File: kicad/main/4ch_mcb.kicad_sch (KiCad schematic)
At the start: 19 parts, among them J15 ICSP, J16 MD1, J17 MD2, J18 MD3, J19 MD4, U5 ATmega328P-AU, Y1 8Mhz

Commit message: fix:
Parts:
- renumbered J15 to J14, J16 to J15, J17 to J16, J18 to J17, J19 to J18
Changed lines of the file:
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@@
   (symbol (lib_id "power:GND") (at 138.43 59.69 0) (unit 1)
     (in_bom yes) (on_board yes)
-    (property "Reference" "#PWR051" (id 0) (at 138.43 66.04 0)
+    (property "Reference" "#PWR049" (id 0) (at 138.43 66.04 0)
       (effects (font (size 1.27 1.27)) hide)
     )
@@
   (symbol (lib_id "Connector_Generic:Conn_01x04") (at 195.58 114.3 0) (unit 1)
     (in_bom yes) (on_board yes)
-    (property "Reference" "J18" (id 0) (at 193.4972 106.2482 0))
+    (property "Reference" "J17" (id 0) (at 193.4972 106.2482 0))
     (property "Value" "MD3" (id 1) (at 193.4972 108.5596 0))
     (property "Footprint" "0.main.robot:JSTB4B-ZR" (id 2) (at 195.58 114.3 0)
@@
   (symbol (lib_id "power:GND") (at 154.94 38.1 0) (unit 1)
     (in_bom yes) (on_board yes)
-    (property "Reference" "#PWR053" (id 0) (at 154.94 44.45 0)
+    (property "Reference" "#PWR051" (id 0) (at 154.94 44.45 0)
       (effects (font (size 1.27 1.27)) hide)
     )
@@
   (symbol (lib_id "power:GND") (at 153.67 106.68 0) (unit 1)
     (in_bom yes) (on_board yes)
-    (property "Reference" "#PWR052" (id 0) (at 153.67 113.03 0)
+    (property "Reference" "#PWR050" (id 0) (at 153.67 113.03 0)
       (effects (font (size 1.27 1.27)) hide)
     )
@@
   (symbol (lib_id "power:+3.3VA") (at 68.58 123.19 0) (unit 1)
     (in_bom yes) (on_board yes)
-    (property "Reference" "#PWR046" (id 0) (at 68.58 127 0)
+    (property "Reference" "#PWR044" (id 0) (at 68.58 127 0)
       (effects (font (size 1.27 1.27)) hide)
     )
@@
   (symbol (lib_id "power:+3.3VA") (at 137.16 39.37 0) (unit 1)
     (in_bom yes) (on_board yes) (fields_autoplaced)
-    (property "Reference" "#PWR050" (id 0) (at 137.16 43.18 0)
+    (property "Reference" "#PWR048" (id 0) (at 137.16 43.18 0)
       (effects (font (size 1.27 1.27)) hide)
     )
@@
   (symbol (lib_id "power:GND") (at 68.58 171.45 0) (unit 1)
     (in_bom yes) (on_board yes)
-    (property "Reference" "#PWR047" (id 0) (at 68.58 177.8 0)
+    (property "Reference" "#PWR045" (id 0) (at 68.58 177.8 0)
       (effects (font (size 1.27 1.27)) hide)
     )
@@
   (symbol (lib_id "Connector_Generic:Conn_01x04") (at 195.58 88.9 0) (unit 1)
     (in_bom yes) (on_board yes)
-    (property "Reference" "J17" (id 0) (at 193.4972 80.8482 0))
+    (property "Reference" "J16" (id 0) (at 193.4972 80.8482 0))
     (property "Value" "MD2" (id 1) (at 193.4972 83.1596 0))
     (property "Footprint" "0.main.robot:JSTB4B-ZR" (id 2) (at 195.58 88.9 0)
@@
   (symbol (lib_id "Connector_Generic:Conn_01x04") (at 195.58 48.26 0) (unit 1)
     (in_bom yes) (on_board yes)
-    (property "Reference" "J16" (id 0) (at 193.4972 40.2082 0))
+    (property "Reference" "J15" (id 0) (at 193.4972 40.2082 0))
     (property "Value" "MD1" (id 1) (at 193.4972 42.5196 0))
     (property "Footprint" "0.main.robot:JSTB4B-ZR" (id 2) (at 195.58 48.26 0)
@@
   (symbol (lib_id "power:+3.3VA") (at 93.98 29.21 0) (unit 1)
     (in_bom yes) (on_board yes) (fields_autoplaced)
-    (property "Reference" "#PWR048" (id 0) (at 93.98 33.02 0)
+    (property "Reference" "#PWR046" (id 0) (at 93.98 33.02 0)
       (effects (font (size 1.27 1.27)) hide)
     )
@@
   (symbol (lib_id "power:+3.3VA") (at 158.75 74.93 0) (unit 1)
     (in_bom yes) (on_board yes) (fields_autoplaced)
-    (property "Reference" "#PWR054" (id 0) (at 158.75 78.74 0)
+    (property "Reference" "#PWR052" (id 0) (at 158.75 78.74 0)
       (effects (font (size 1.27 1.27)) hide)
     )
@@
   (symbol (lib_id "Connector_Generic:Conn_01x04") (at 195.58 130.81 0) (unit 1)
     (in_bom yes) (on_board yes)
-    (property "Reference" "J19" (id 0) (at 193.4972 122.7582 0))
+    (property "Reference" "J18" (id 0) (at 193.4972 122.7582 0))
     (property "Value" "MD4" (id 1) (at 193.4972 125.0696 0))
     (property "Footprint" "0.main.robot:JSTB4B-ZR" (id 2) (at 195.58 130.81 0)
@@
   (symbol (lib_id "Connector_Generic:Conn_01x06") (at 147.32 30.48 90) (unit 1)
     (in_bom yes) (on_board yes)
-    (property "Reference" "J15" (id 0) (at 157.1752 31.3944 90)
+    (property "Reference" "J14" (id 0) (at 157.1752 31.3944 90)
       (effects (font (size 1.27 1.27)) (justify right))
     )
@@
   (symbol (lib_id "power:GND") (at 49.53 120.65 0) (unit 1)
     (in_bom yes) (on_board yes)
-    (property "Reference" "#PWR045" (id 0) (at 49.53 127 0)
+    (property "Reference" "#PWR043" (id 0) (at 49.53 127 0)
       (effects (font (size 1.27 1.27)) hide)
     )
@@
   (symbol (lib_id "power:GND") (at 127 96.52 0) (unit 1)
     (in_bom yes) (on_board yes)
-    (property "Reference" "#PWR049" (id 0) (at 127 102.87 0)
-      (effects (font (size 1.27 1.27)) hide)
-    )
+    (property "Reference" "#PWR047" (id 0) (at 127 102.87 0)
+      (effects (font (size 1.27 1.27)) hide)
+    )

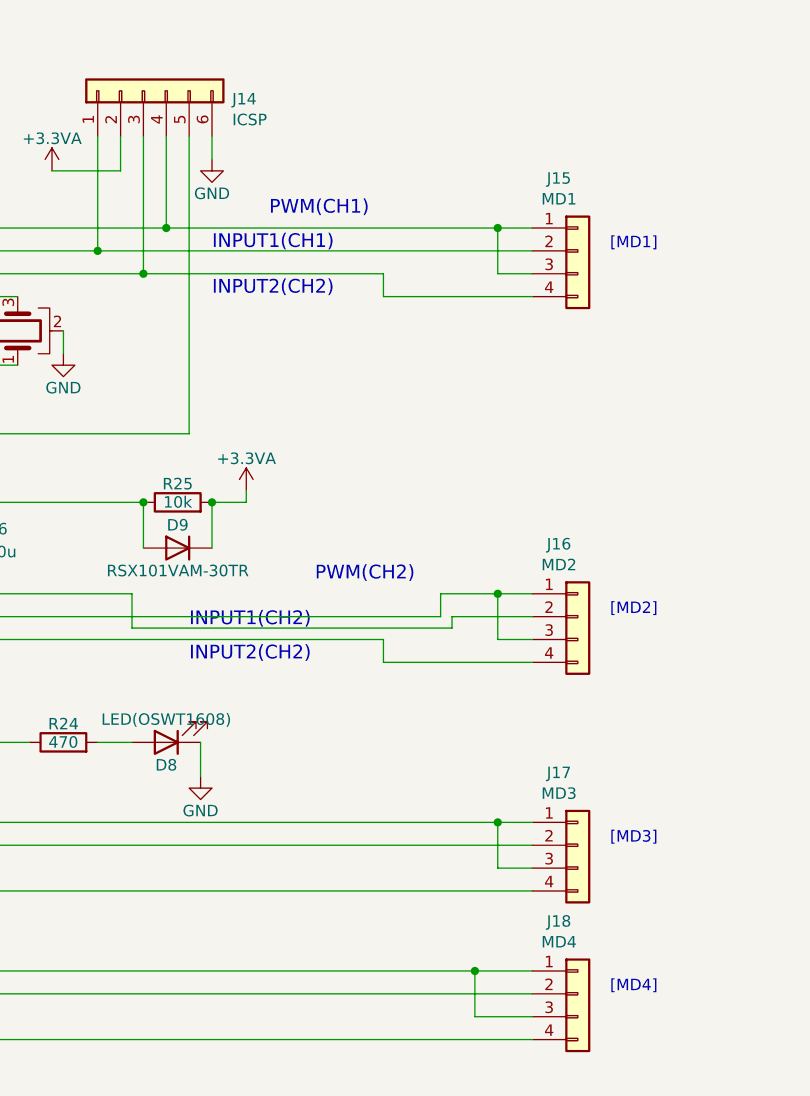
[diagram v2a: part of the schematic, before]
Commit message: fix: vison-board GND
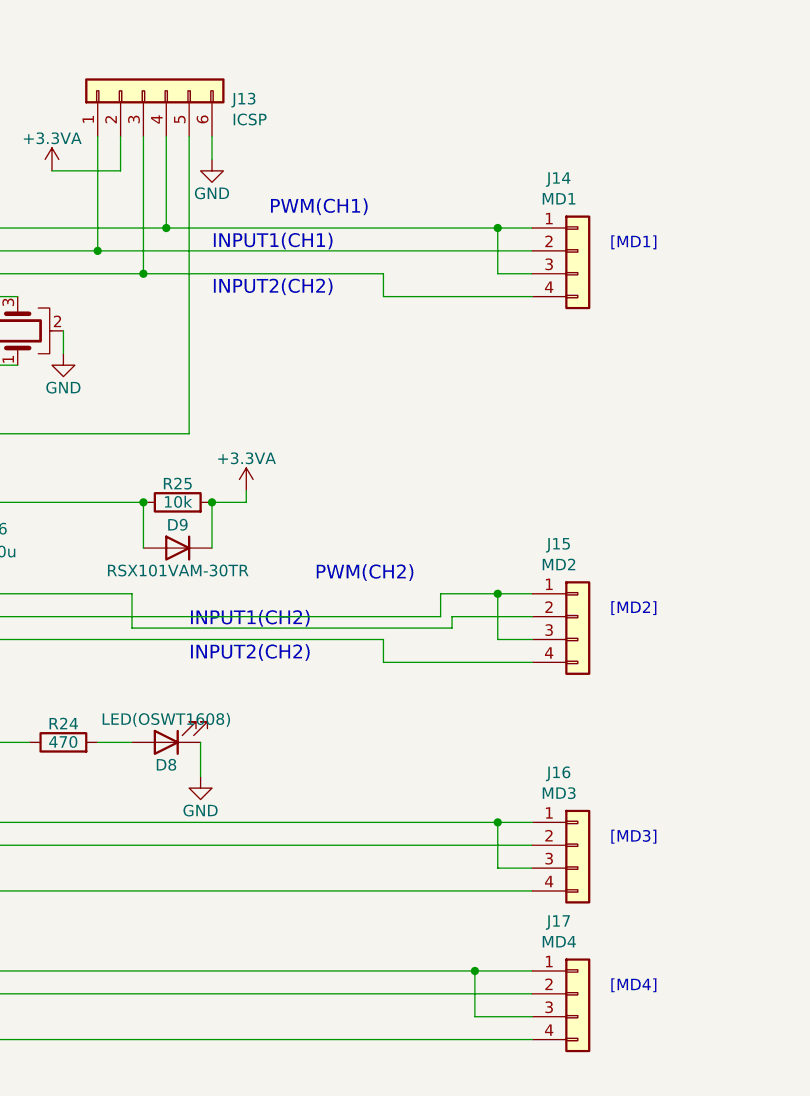
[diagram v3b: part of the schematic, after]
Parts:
- renumbered J14 to J13, J15 to J14, J16 to J15, J17 to J16, J18 to J17
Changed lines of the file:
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@@
   (symbol (lib_id "power:GND") (at 138.43 59.69 0) (unit 1)
     (in_bom yes) (on_board yes)
-    (property "Reference" "#PWR049" (id 0) (at 138.43 66.04 0)
+    (property "Reference" "#PWR048" (id 0) (at 138.43 66.04 0)
       (effects (font (size 1.27 1.27)) hide)
     )
@@
   (symbol (lib_id "Connector_Generic:Conn_01x04") (at 195.58 114.3 0) (unit 1)
     (in_bom yes) (on_board yes)
-    (property "Reference" "J17" (id 0) (at 193.4972 106.2482 0))
+    (property "Reference" "J16" (id 0) (at 193.4972 106.2482 0))
     (property "Value" "MD3" (id 1) (at 193.4972 108.5596 0))
     (property "Footprint" "0.main.robot:JSTB4B-ZR" (id 2) (at 195.58 114.3 0)
@@
   (symbol (lib_id "power:GND") (at 154.94 38.1 0) (unit 1)
     (in_bom yes) (on_board yes)
-    (property "Reference" "#PWR051" (id 0) (at 154.94 44.45 0)
+    (property "Reference" "#PWR050" (id 0) (at 154.94 44.45 0)
       (effects (font (size 1.27 1.27)) hide)
     )
@@
   (symbol (lib_id "power:GND") (at 153.67 106.68 0) (unit 1)
     (in_bom yes) (on_board yes)
-    (property "Reference" "#PWR050" (id 0) (at 153.67 113.03 0)
+    (property "Reference" "#PWR049" (id 0) (at 153.67 113.03 0)
       (effects (font (size 1.27 1.27)) hide)
     )
@@
   (symbol (lib_id "power:+3.3VA") (at 68.58 123.19 0) (unit 1)
     (in_bom yes) (on_board yes)
-    (property "Reference" "#PWR044" (id 0) (at 68.58 127 0)
+    (property "Reference" "#PWR043" (id 0) (at 68.58 127 0)
       (effects (font (size 1.27 1.27)) hide)
     )
@@
   (symbol (lib_id "power:+3.3VA") (at 137.16 39.37 0) (unit 1)
     (in_bom yes) (on_board yes) (fields_autoplaced)
-    (property "Reference" "#PWR048" (id 0) (at 137.16 43.18 0)
+    (property "Reference" "#PWR047" (id 0) (at 137.16 43.18 0)
       (effects (font (size 1.27 1.27)) hide)
     )
@@
   (symbol (lib_id "power:GND") (at 68.58 171.45 0) (unit 1)
     (in_bom yes) (on_board yes)
-    (property "Reference" "#PWR045" (id 0) (at 68.58 177.8 0)
+    (property "Reference" "#PWR044" (id 0) (at 68.58 177.8 0)
       (effects (font (size 1.27 1.27)) hide)
     )
@@
   (symbol (lib_id "Connector_Generic:Conn_01x04") (at 195.58 88.9 0) (unit 1)
     (in_bom yes) (on_board yes)
-    (property "Reference" "J16" (id 0) (at 193.4972 80.8482 0))
+    (property "Reference" "J15" (id 0) (at 193.4972 80.8482 0))
     (property "Value" "MD2" (id 1) (at 193.4972 83.1596 0))
     (property "Footprint" "0.main.robot:JSTB4B-ZR" (id 2) (at 195.58 88.9 0)
@@
   (symbol (lib_id "Connector_Generic:Conn_01x04") (at 195.58 48.26 0) (unit 1)
     (in_bom yes) (on_board yes)
-    (property "Reference" "J15" (id 0) (at 193.4972 40.2082 0))
+    (property "Reference" "J14" (id 0) (at 193.4972 40.2082 0))
     (property "Value" "MD1" (id 1) (at 193.4972 42.5196 0))
     (property "Footprint" "0.main.robot:JSTB4B-ZR" (id 2) (at 195.58 48.26 0)
@@
   (symbol (lib_id "power:+3.3VA") (at 93.98 29.21 0) (unit 1)
     (in_bom yes) (on_board yes) (fields_autoplaced)
-    (property "Reference" "#PWR046" (id 0) (at 93.98 33.02 0)
+    (property "Reference" "#PWR045" (id 0) (at 93.98 33.02 0)
       (effects (font (size 1.27 1.27)) hide)
     )
@@
   (symbol (lib_id "power:+3.3VA") (at 158.75 74.93 0) (unit 1)
     (in_bom yes) (on_board yes) (fields_autoplaced)
-    (property "Reference" "#PWR052" (id 0) (at 158.75 78.74 0)
+    (property "Reference" "#PWR051" (id 0) (at 158.75 78.74 0)
       (effects (font (size 1.27 1.27)) hide)
     )
@@
   (symbol (lib_id "Connector_Generic:Conn_01x04") (at 195.58 130.81 0) (unit 1)
     (in_bom yes) (on_board yes)
-    (property "Reference" "J18" (id 0) (at 193.4972 122.7582 0))
+    (property "Reference" "J17" (id 0) (at 193.4972 122.7582 0))
     (property "Value" "MD4" (id 1) (at 193.4972 125.0696 0))
     (property "Footprint" "0.main.robot:JSTB4B-ZR" (id 2) (at 195.58 130.81 0)
@@
   (symbol (lib_id "Connector_Generic:Conn_01x06") (at 147.32 30.48 90) (unit 1)
     (in_bom yes) (on_board yes)
-    (property "Reference" "J14" (id 0) (at 157.1752 31.3944 90)
+    (property "Reference" "J13" (id 0) (at 157.1752 31.3944 90)
       (effects (font (size 1.27 1.27)) (justify right))
     )
@@
   (symbol (lib_id "power:GND") (at 49.53 120.65 0) (unit 1)
     (in_bom yes) (on_board yes)
-    (property "Reference" "#PWR043" (id 0) (at 49.53 127 0)
+    (property "Reference" "#PWR042" (id 0) (at 49.53 127 0)
       (effects (font (size 1.27 1.27)) hide)
     )
@@
   (symbol (lib_id "power:GND") (at 127 96.52 0) (unit 1)
     (in_bom yes) (on_board yes)
-    (property "Reference" "#PWR047" (id 0) (at 127 102.87 0)
-      (effects (font (size 1.27 1.27)) hide)
-    )
+    (property "Reference" "#PWR046" (id 0) (at 127 102.87 0)
+      (effects (font (size 1.27 1.27)) hide)
+    )

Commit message: fix: main 配線前
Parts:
- J14, J15, J16, J17: footprint 0.main.robot:JSTB4B-ZR -> 0.main.robot:JSTS4B-ZRLFSN
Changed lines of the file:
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@@
     (property "Reference" "J16" (id 0) (at 193.4972 106.2482 0))
     (property "Value" "MD3" (id 1) (at 193.4972 108.5596 0))
-    (property "Footprint" "0.main.robot:JSTB4B-ZR" (id 2) (at 195.58 114.3 0)
+    (property "Footprint" "0.main.robot:JSTS4B-ZRLFSN" (id 2) (at 195.58 114.3 0)
       (effects (font (size 1.27 1.27)) hide)
     )
@@
     (property "Reference" "J15" (id 0) (at 193.4972 80.8482 0))
     (property "Value" "MD2" (id 1) (at 193.4972 83.1596 0))
-    (property "Footprint" "0.main.robot:JSTB4B-ZR" (id 2) (at 195.58 88.9 0)
+    (property "Footprint" "0.main.robot:JSTS4B-ZRLFSN" (id 2) (at 195.58 88.9 0)
       (effects (font (size 1.27 1.27)) hide)
     )
@@
     (property "Reference" "J14" (id 0) (at 193.4972 40.2082 0))
     (property "Value" "MD1" (id 1) (at 193.4972 42.5196 0))
-    (property "Footprint" "0.main.robot:JSTB4B-ZR" (id 2) (at 195.58 48.26 0)
+    (property "Footprint" "0.main.robot:JSTS4B-ZRLFSN" (id 2) (at 195.58 48.26 0)
       (effects (font (size 1.27 1.27)) hide)
     )
@@
     (property "Reference" "J17" (id 0) (at 193.4972 122.7582 0))
     (property "Value" "MD4" (id 1) (at 193.4972 125.0696 0))
-    (property "Footprint" "0.main.robot:JSTB4B-ZR" (id 2) (at 195.58 130.81 0)
-      (effects (font (size 1.27 1.27)) hide)
-    )
+    (property "Footprint" "0.main.robot:JSTS4B-ZRLFSN" (id 2) (at 195.58 130.81 0)
+      (effects (font (size 1.27 1.27)) hide)
+    )
